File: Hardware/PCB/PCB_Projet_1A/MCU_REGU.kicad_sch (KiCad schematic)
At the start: 18 parts, among them J13 Conn_01x02, J14 BU33SD5WG-TR, J15 R-78B5.0-2.0, U3 STM32L552CCTx

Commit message: Avancement sur le PCB editor
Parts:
- J13: footprint Connector_JST:JST_XH_S2B-XH-A-1_1x02_P2.50mm_Horizontal -> Connector_JST:JST_XH_B2B-XH-A_1x02_P2.50mm_Vertical
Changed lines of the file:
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@@
 			)
 		)
-		(property "Footprint" "Connector_JST:JST_XH_S2B-XH-A-1_1x02_P2.50mm_Horizontal"
+		(property "Footprint" "Connector_JST:JST_XH_B2B-XH-A_1x02_P2.50mm_Vertical"
 			(at 177.8 67.31 0)
 			(effects

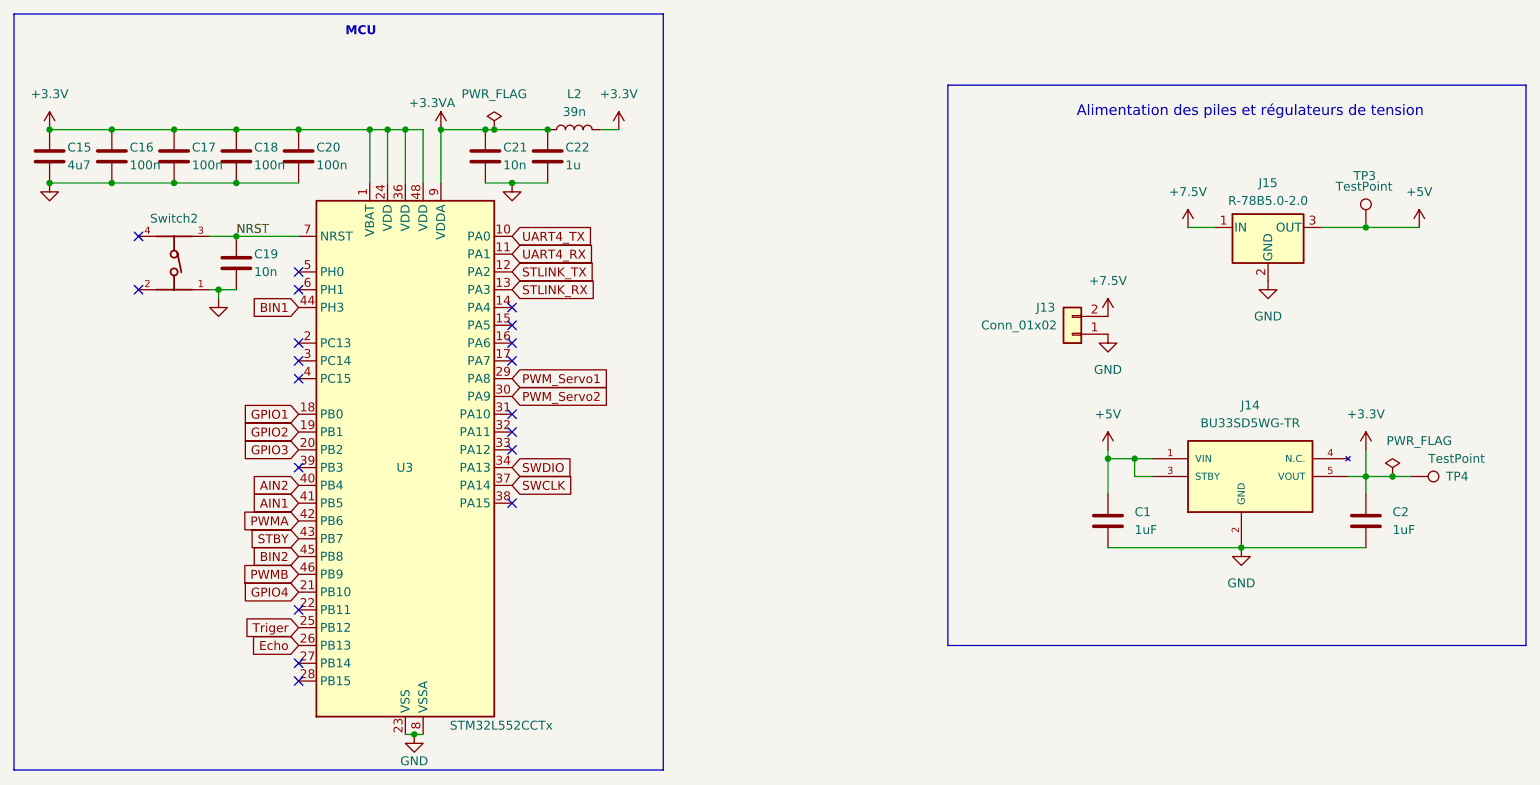
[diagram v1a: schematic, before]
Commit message: Finalisation du PCB et ajout du README dans le répertoire PCB
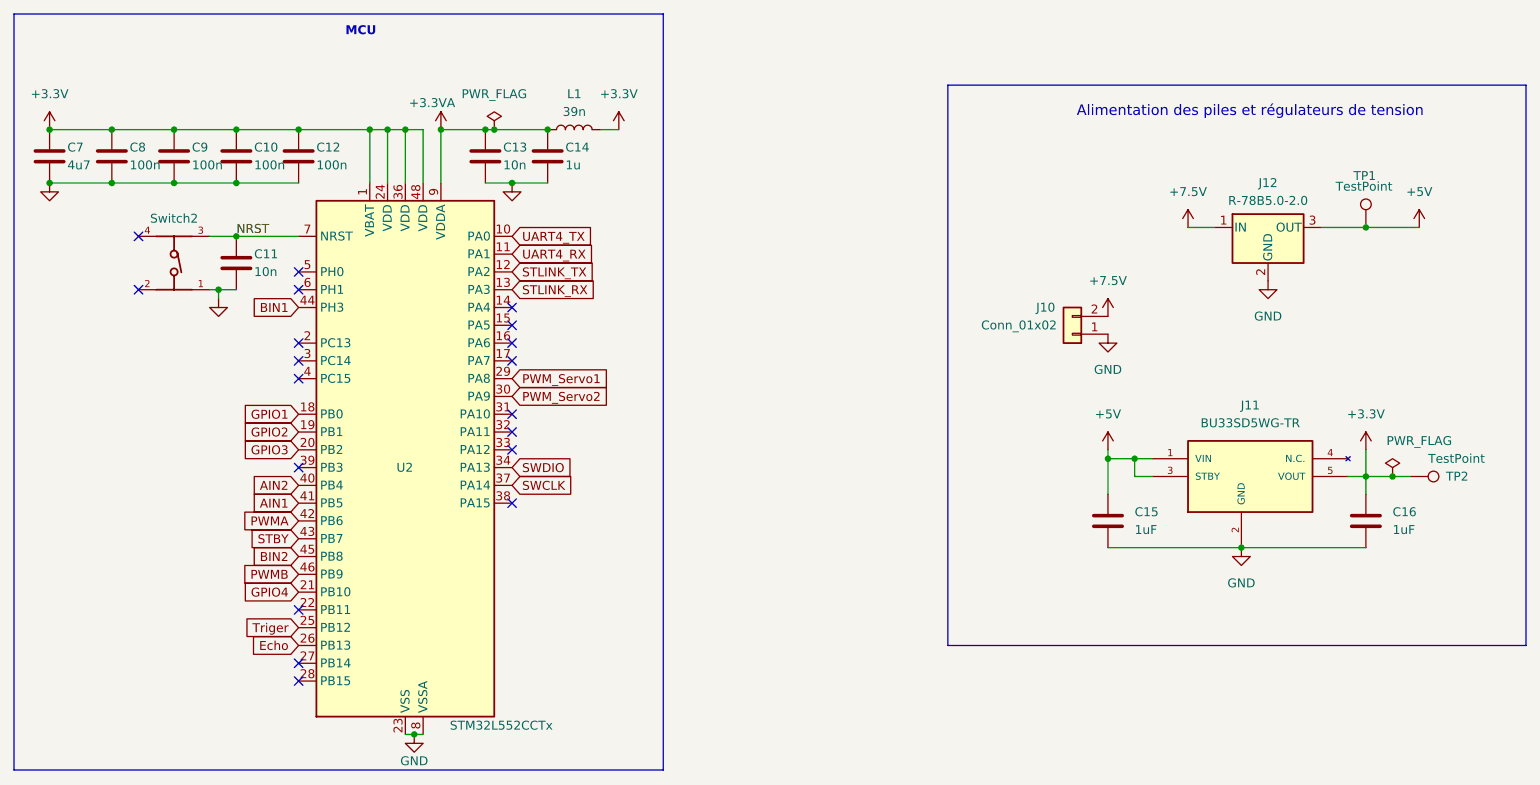
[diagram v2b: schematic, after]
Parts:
- renumbered C18 to C10, C19 to C11, C20 to C12, C21 to C13, C22 to C14, C1 to C15, C2 to C16, C15 to C7, C16 to C8, C17 to C9, J13 to J10, J14 to J11, J15 to J12, L2 to L1, TP3 to TP1, TP4 to TP2, U3 to U2

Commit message: modif pcb
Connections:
- net UART3_RX: now reaches U2.22 (PB11)
- net GPIO4 renamed UART3_TX
- no-connect marks 19 -> 18
